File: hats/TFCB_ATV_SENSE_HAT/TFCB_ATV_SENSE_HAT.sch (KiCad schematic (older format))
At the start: 0 parts

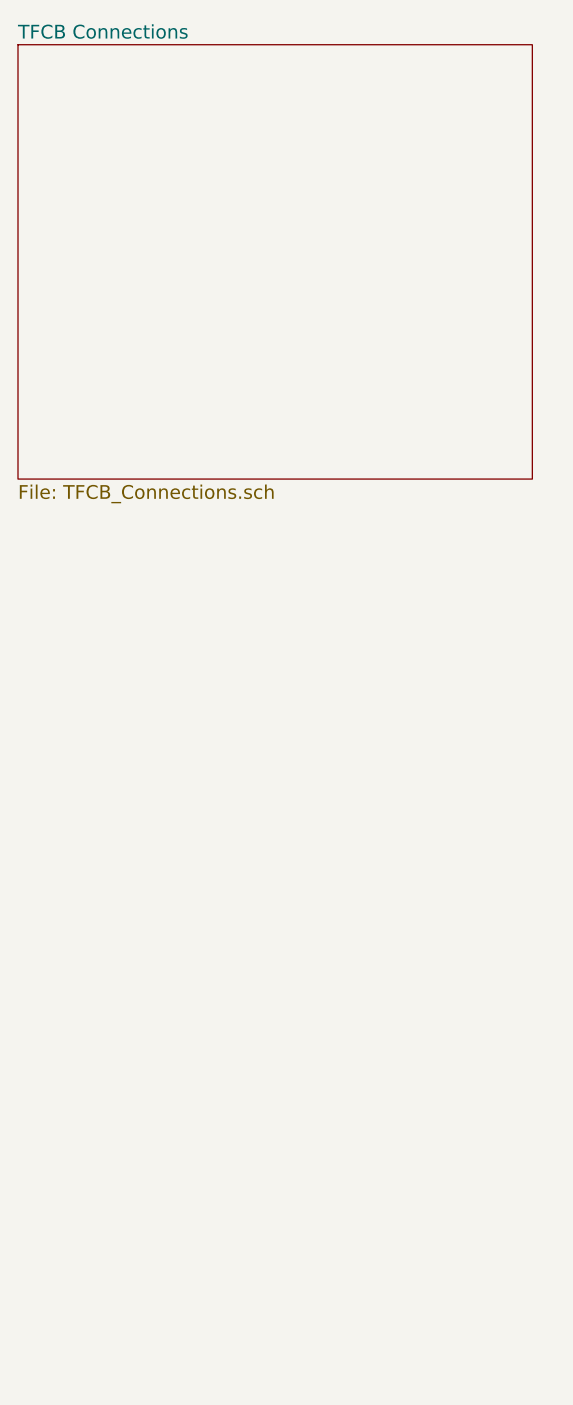
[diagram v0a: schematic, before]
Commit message: Moved power regulators to top side and corrected bad package
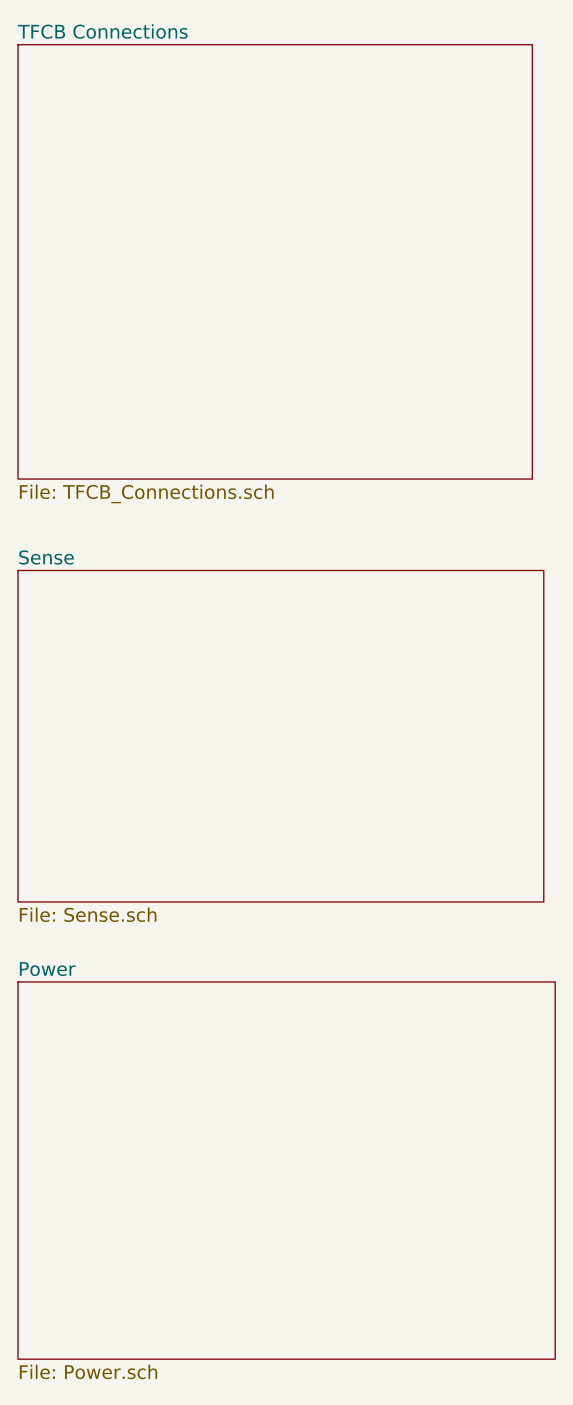
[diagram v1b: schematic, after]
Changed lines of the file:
@@
 $Descr A4 11693 8268
 encoding utf-8
-Sheet 1 2
+Sheet 1 4
 Title ""
 Date ""
@@
 F1 "TFCB_Connections.sch" 60
 $EndSheet
+$Sheet
+S 750  3250 2300 1450
+U 55E6B920
+F0 "Sense" 60
+F1 "Sense.sch" 60
+$EndSheet
+$Sheet
+S 750  5050 2350 1650
+U 55E7057D
+F0 "Power" 60
+F1 "Power.sch" 60
+$EndSheet
 $EndSCHEMATC
